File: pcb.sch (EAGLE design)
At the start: 29 parts, among them IC1 16-HTSSOP-DRV8833, IC10 SOT-23-6"S-8261, IC9 BQ24092, Q1 SOT-223, Q2 SOT-23-6L

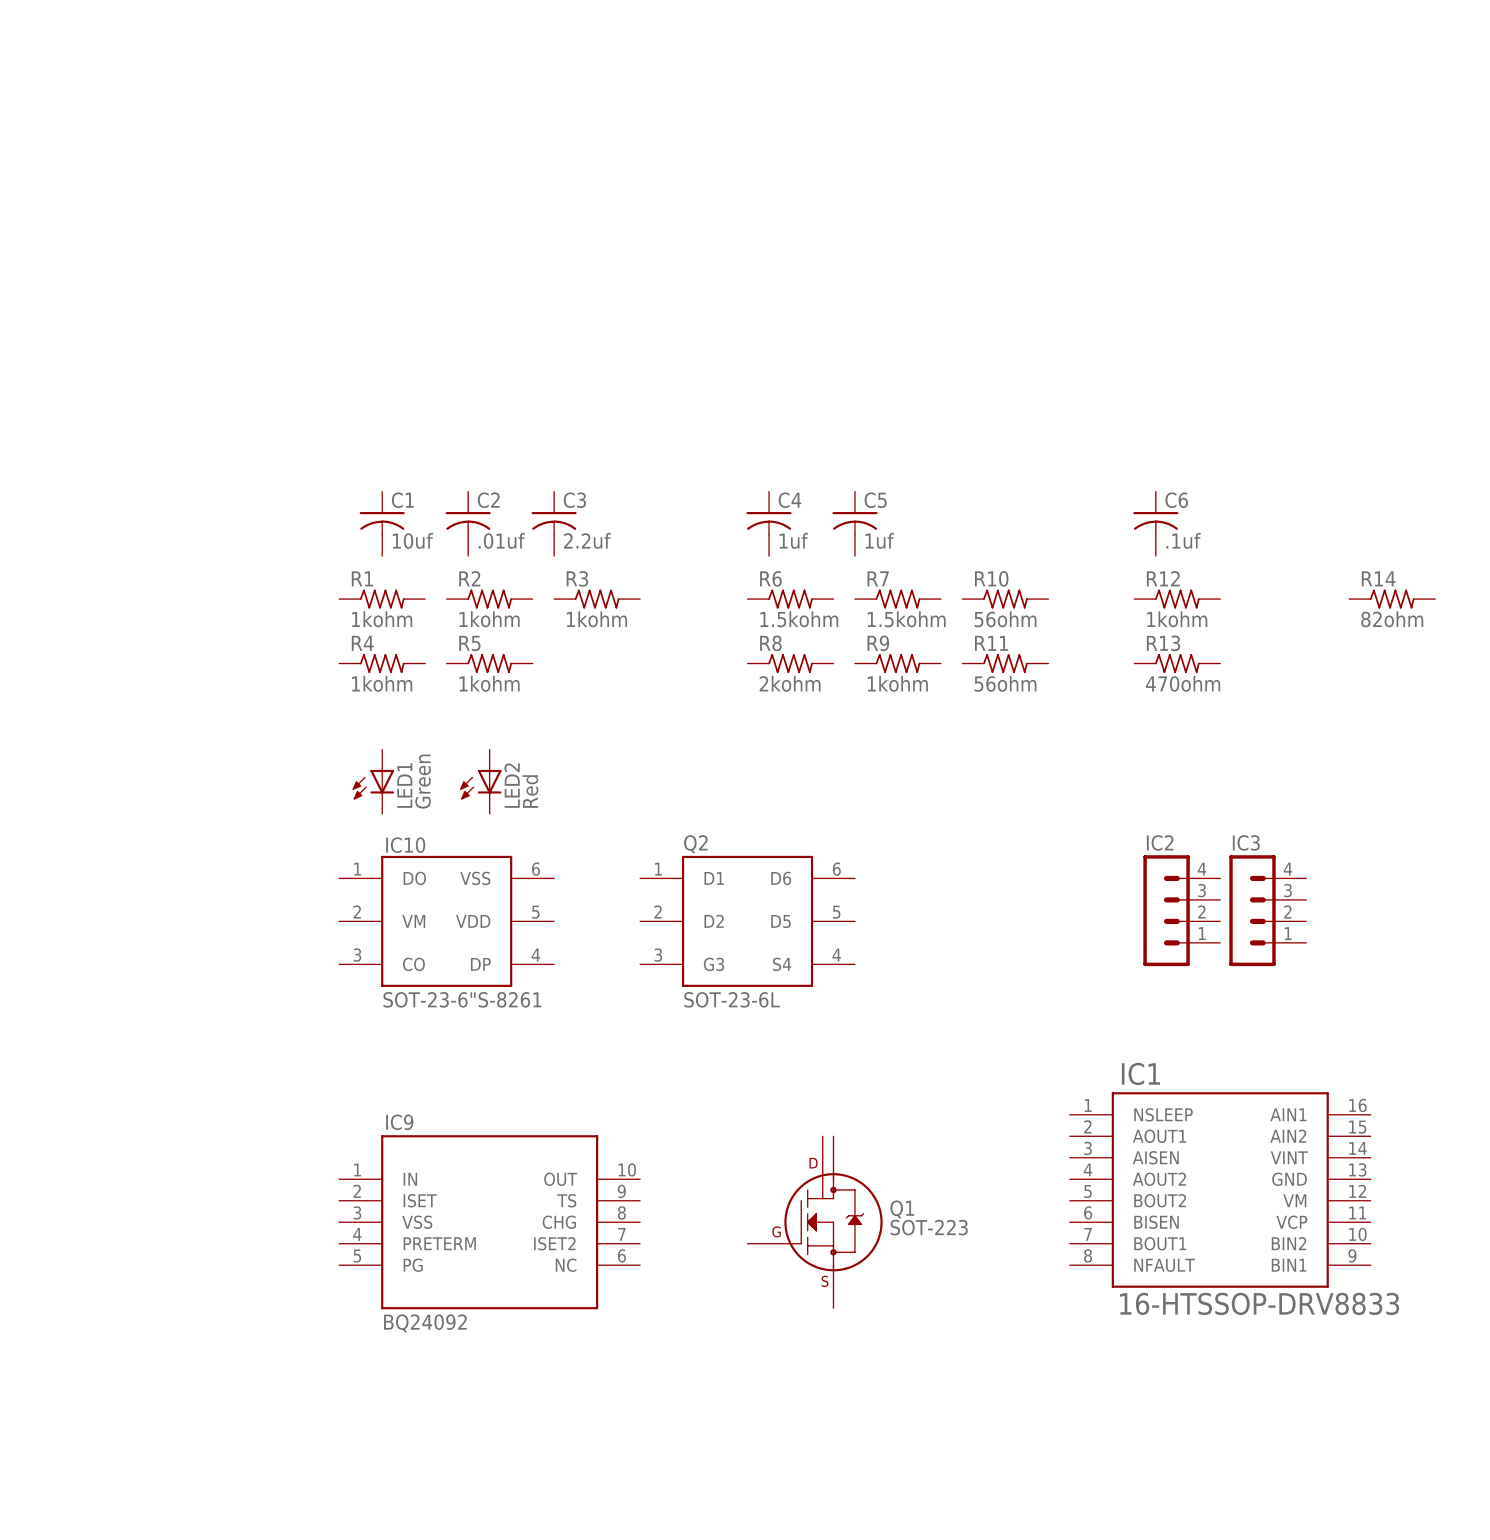
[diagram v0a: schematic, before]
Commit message: Preliminary PCB schematic and stamp module layout
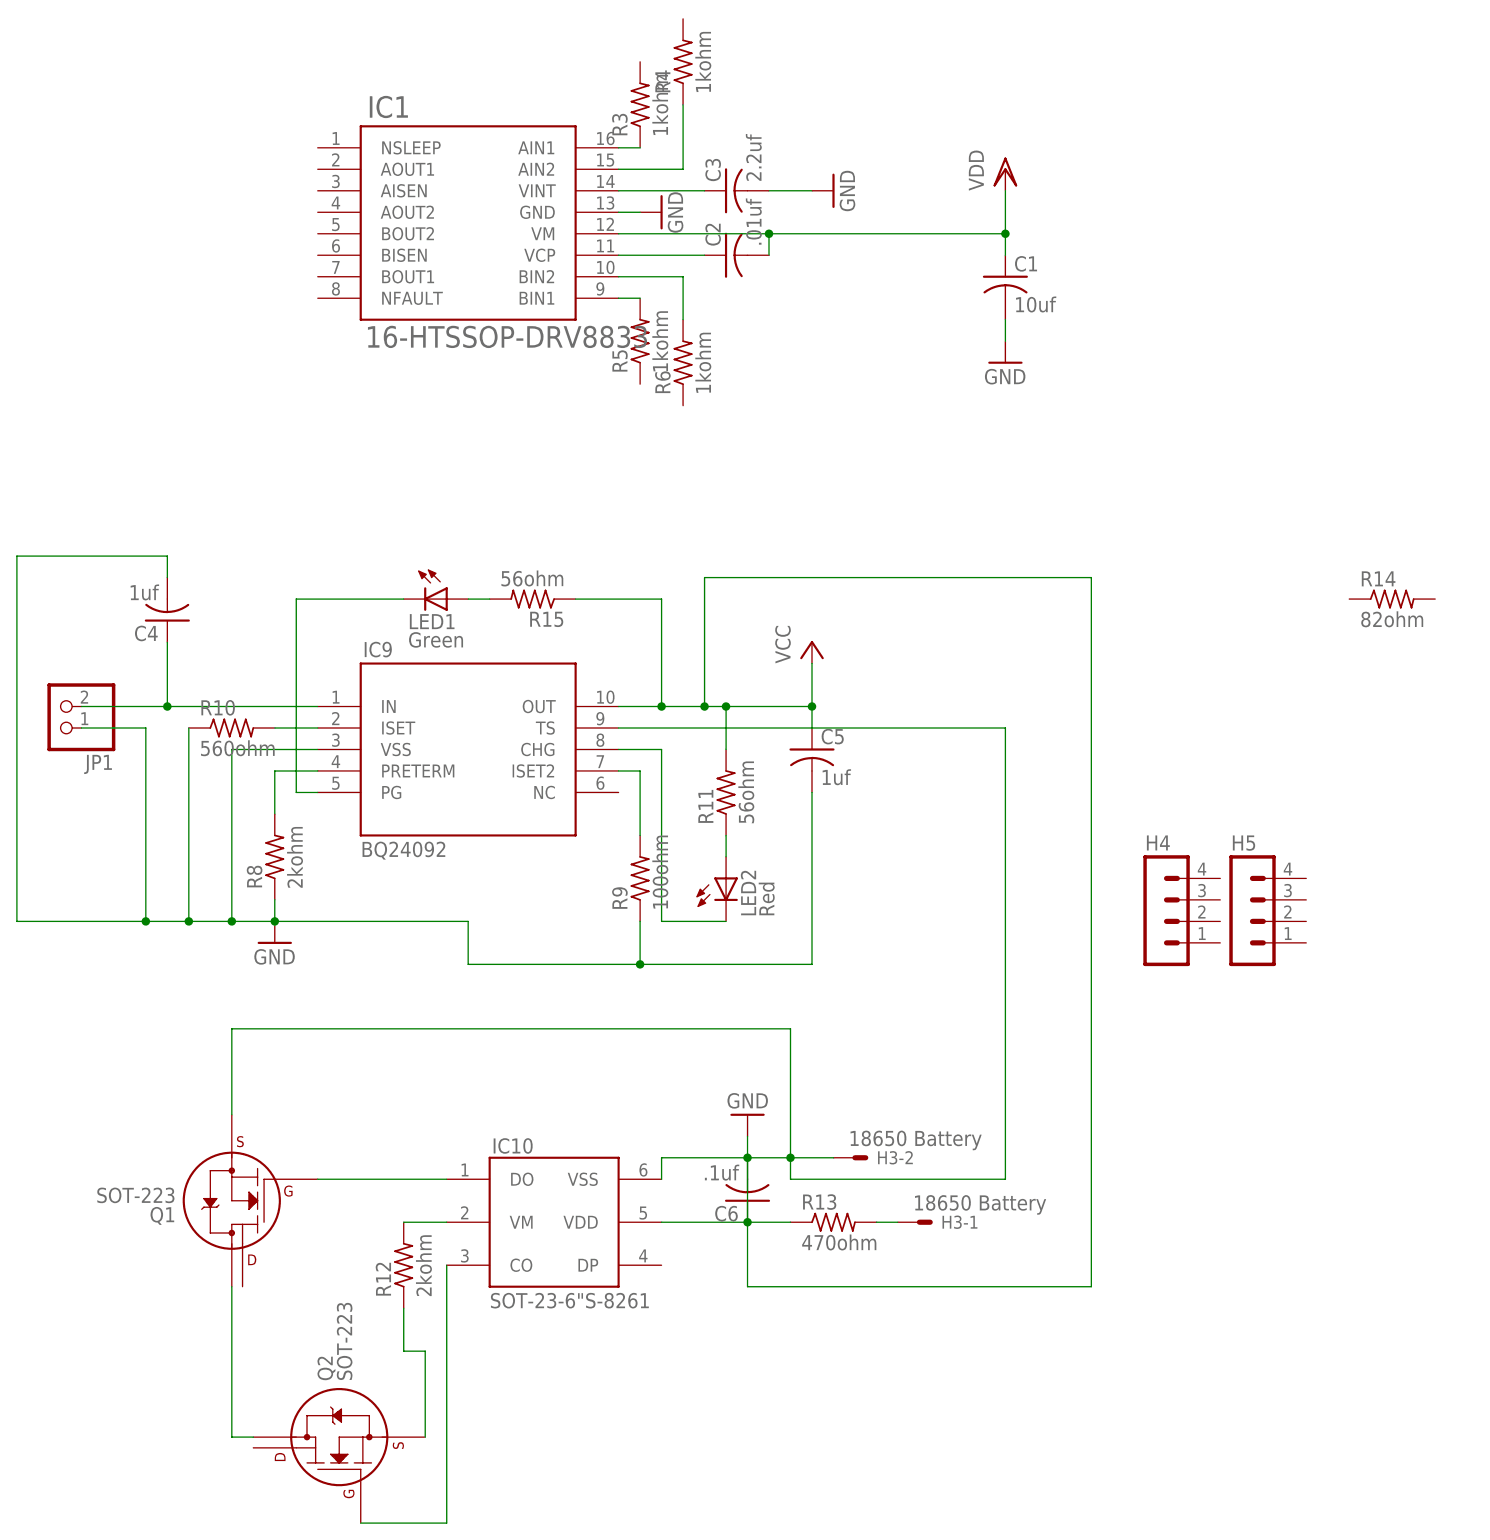
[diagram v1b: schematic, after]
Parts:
- removed R1, R2: 1kohm, rcl:R-US_R0805
- removed R7: 1.5kohm, rcl:R-US_R1206
- added H3: 18650 Battery, con-molex:KK-156-2
- added JP1: (no value), pinhead:PINHD-1X2
- added R15: 56ohm, rcl:R-US_R1206
- Q2: value SOT-23-6L -> SOT-223; device ECE477_project:SOT-23-6L -> transistors:IRLL014
- R10: value 56ohm -> 560ohm
- R12: value 1kohm -> 2kohm
- R6: value 1.5kohm -> 1kohm; device rcl:R-US_R1206 -> rcl:R-US_R0805
- R9: value 1kohm -> 100ohm
- renumbered IC2 to H4, IC3 to H5
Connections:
- new net GND: C1.2, C3.2, C4.2, C5.1, C5.2, C6.1, C6.2, H3-2.S, IC1.GND, IC10.VDD, IC10.VSS, IC9.OUT, IC9.TS, IC9.VSS, JP1.1, Q1.S, R10.1, R11.2, R13.1, R15.1, R8.1, R9.1
- new net N$1: C3.1, IC1.VINT
- new net N$10: IC9.ISET, R10.2
- new net N$11: IC9.PRETERM, R8.2
- new net N$12: IC10.DO, Q1.G
- new net N$13: C4.1, IC9.IN, JP1.2
- new net N$14: IC1.BIN1, R5.2
- new net N$15: IC10.CO, Q2.G
- new net N$16: Q1.D1, Q2.D1
- new net N$17: IC9.ISET2, R9.2
- new net N$18: H3-1.S, R13.2
- new net N$19: Q2.S, R12.1
- new net N$2: IC10.VM, R12.2
- new net N$20: IC1.BIN2, R6.2
- new net N$3: C2.1, IC1.VCP
- new net N$4: IC1.AIN1, R3.1
- new net N$5: IC1.AIN2, R4.1
- new net N$6: IC9.PG, LED1.C
- new net N$7: LED1.A, R15.2
- new net N$8: IC9.CHG, LED2.C
- new net N$9: LED2.A, R11.1
- new net VDD: C1.1, C2.2, IC1.VM
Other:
- moved on the sheet: C1, C2, C3, C4, C5, C6, IC1, IC10, IC9, LED1, LED2, Q1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
